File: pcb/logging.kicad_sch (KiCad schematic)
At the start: 14 parts, among them J6 MSD-4-A, U12 W25Q128JVS

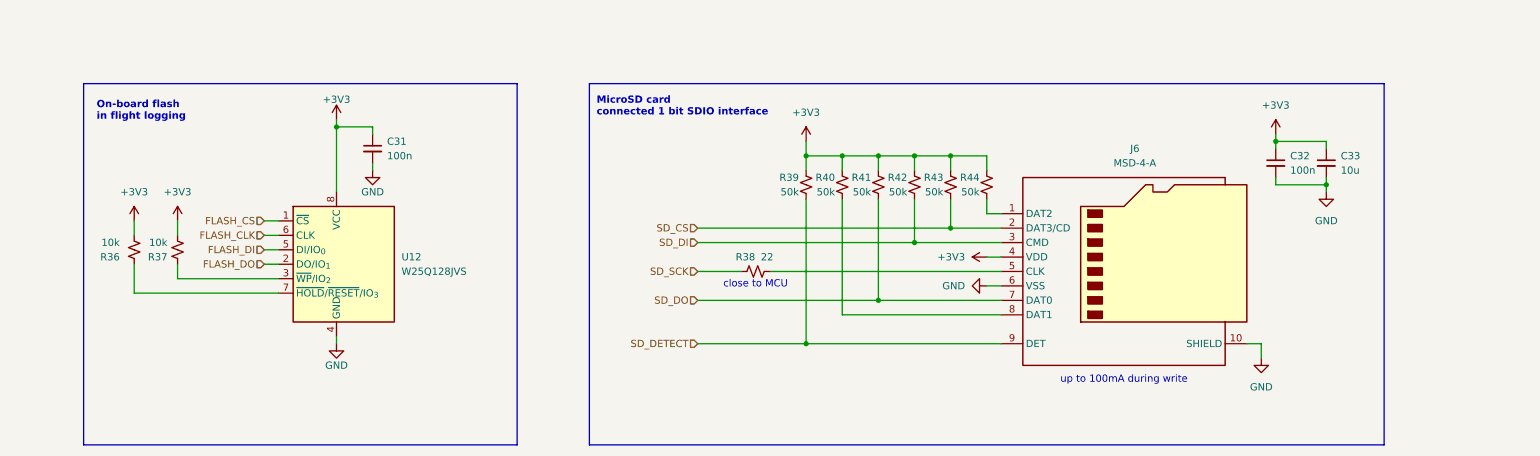
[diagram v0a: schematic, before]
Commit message: Improve inter sheet connections
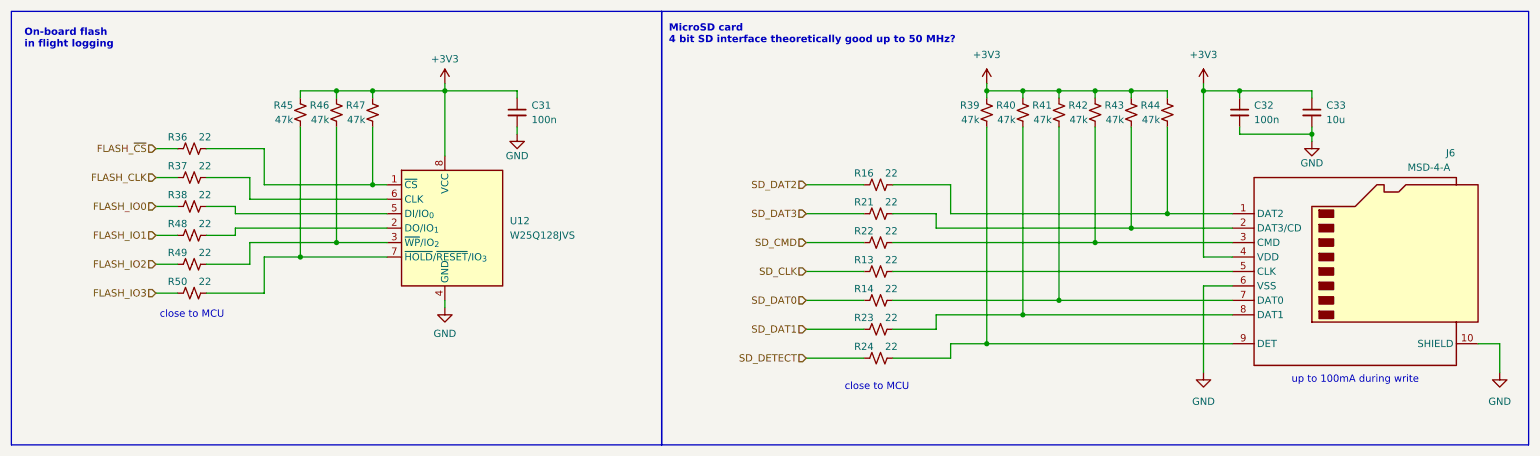
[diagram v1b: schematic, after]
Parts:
- added R13, R14, R16, R21, R22, R23, R24, R48, R49, R50: 22, symbol Device:R_Small_US
- added R45, R46, R47: 47k, symbol Device:R_Small_US
- R36, R37: value 10k -> 22
- R39, R40, R41, R42, R43, R44: value 50k -> 47k
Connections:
- net FLASH_DI is gone; now on an unnamed net: U12.5 (DI/IO_{0})
- net +3V3: now also R45.1, R46.1, R47.1; no longer R36.1, R37.1
- net FLASH_CLK: now also R37.1; no longer U12.6 (CLK)
- net SD_DETECT: now also R24.1; no longer J6.9 (DET), R39.2
- net at J6.1 (DAT2), R44.2: now also R16.2
- net at R38.2: no longer J6.5 (CLK)
- net at J6.8 (DAT1), R40.2: now also R23.2
- net at R37.2: now also U12.6 (CLK); no longer U12.3 (~{WP}/IO_{2})
- net at U12.7 (~{HOLD}/~{RESET}/IO_{3}): now also R45.2, R50.2; no longer R36.2
- net FLASH_CS: no longer names the net of U12.1 (~{CS})
- net FLASH_CS: now also R36.2, R47.2
- net FLASH_DO: no longer names the net of U12.2 (DO/IO_{1})
- net FLASH_DO: now also R48.2
- net SD_CS: no longer names the net of J6.2 (DAT3/CD), R43.2
- net SD_CS: now also R21.2
- net SD_DI: no longer names the net of J6.3 (CMD), R42.2
- net SD_DI: now also R22.2
- net SD_DO: no longer names the net of J6.7 (DAT0), R41.2
- net SD_DO: now also R14.2
- net SD_SCK renamed FLASH_IO0
- new net: R46.2, R49.2, U12.3 (~{WP}/IO_{2})
- new net: J6.9 (DET), R24.2, R39.2
- new net: J6.5 (CLK), R13.2
- new net FLASH_IO1: R48.1
- new net FLASH_IO2: R49.1
- new net FLASH_IO3: R50.1
- new net FLASH_~{CS}: R36.1
- new net SD_CLK: R13.1
- new net SD_CMD: R22.1
- new net SD_DAT0: R14.1
- new net SD_DAT1: R23.1
- new net SD_DAT2: R16.1
- new net SD_DAT3: R21.1
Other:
- note added: "MicroSD card 4 bit SD interface theoretically good up to 50 MHz?"
- note removed: "MicroSD card connected 1 bit SDIO interface"
- title: (none) -> Flight Computer
- moved on the sheet: C31, C32, C33, J6, R39, R40, R41, R42, R43, R44, U12

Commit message: Fix pin directionality
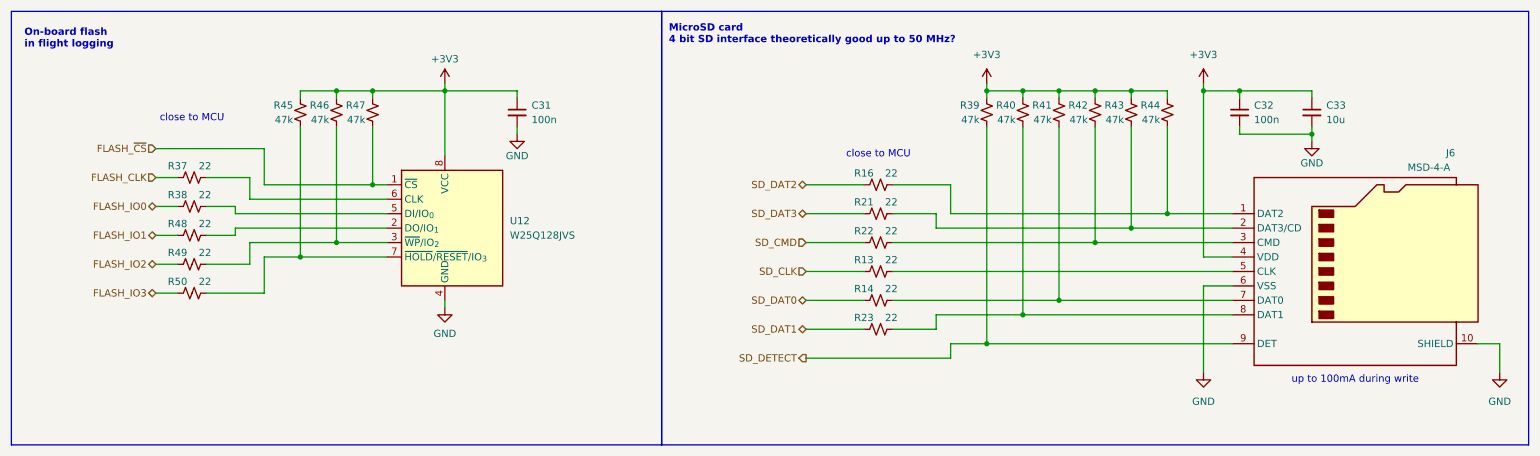
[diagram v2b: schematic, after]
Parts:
- removed R24, R36: 22, symbol Device:R_Small_US
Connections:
- net FLASH_~{CS}: now also R47.2, U12.1 (~{CS})
- net SD_DETECT: now also J6.9 (DET), R39.2
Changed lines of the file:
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@@
 	(text "close to MCU"
 		(exclude_from_sim no)
-		(at 44.45 66.04 0)
+		(at 44.45 31.496 0)
 		(effects
 			(font
@@
 	(text "close to MCU"
 		(exclude_from_sim no)
-		(at 164.846 78.74 0)
+		(at 165.1 37.846 0)
 		(effects
 			(font
@@
 	(wire
 		(pts
-			(xy 46.99 36.83) (xy 57.15 36.83)
-		)
-		(stroke
-			(width 0)
-			(type default)
-		)
-	)
-	(wire
-		(pts
 			(xy 167.64 63.5) (xy 196.85 63.5)
 		)
@@
 	(wire
 		(pts
-			(xy 38.1 36.83) (xy 41.91 36.83)
+			(xy 38.1 36.83) (xy 57.15 36.83)
 		)
 		(stroke
@@
 	(wire
 		(pts
-			(xy 152.4 73.66) (xy 162.56 73.66)
+			(xy 152.4 73.66) (xy 177.8 73.66)
 		)
 		(stroke
@@
 	(wire
 		(pts
-			(xy 167.64 73.66) (xy 177.8 73.66)
-		)
-		(stroke
-			(width 0)
-			(type default)
-		)
-	)
-	(wire
-		(pts
 			(xy 227.33 48.26) (xy 215.9 48.26)
 		)
@@
 	)
 	(hierarchical_label "SD_DETECT"
-		(shape input)
+		(shape output)
 		(at 152.4 73.66 180)
 		(effects
@@
 	)
 	(hierarchical_label "SD_DAT1"
-		(shape input)
+		(shape bidirectional)
 		(at 152.4 68.58 180)
 		(effects
@@
 	)
 	(hierarchical_label "FLASH_IO0"
-		(shape input)
+		(shape bidirectional)
 		(at 38.1 46.99 180)
 		(effects
@@
 	)
 	(hierarchical_label "FLASH_IO3"
-		(shape input)
+		(shape bidirectional)
 		(at 38.1 62.23 180)
 		(effects
@@
 	)
 	(hierarchical_label "FLASH_IO1"
-		(shape input)
+		(shape bidirectional)
 		(at 38.1 52.07 180)
 		(effects
@@
 	)
 	(hierarchical_label "SD_DAT3"
-		(shape input)
+		(shape bidirectional)
 		(at 152.4 48.26 180)
 		(effects
@@
 	)
 	(hierarchical_label "SD_DAT0"
-		(shape input)
+		(shape bidirectional)
 		(at 152.4 63.5 180)
 		(effects
@@
 	)
 	(hierarchical_label "FLASH_IO2"
-		(shape input)
+		(shape bidirectional)
 		(at 38.1 57.15 180)
 		(effects
@@
 	)
 	(hierarchical_label "SD_DAT2"
-		(shape input)
+		(shape bidirectional)
 		(at 152.4 43.18 180)
 		(effects
@@
 	)
 	(symbol
-		(lib_id "Device:R_Small_US")
-		(at 165.1 73.66 90)
-		(unit 1)
-		(exclude_from_sim no)
-		(in_bom yes)
-		(on_board yes)
-		(dnp no)
-		(property "Reference" "R24"
-			(at 162.56 71.628 90)
-			(effects
-				(font
-					(size 1.27 1.27)
-				)
-			)
-		)
-		(property "Value" "22"
-			(at 167.386 71.628 90)
-			(effects
-				(font
-					(size 1.27 1.27)
-				)
-			)
-		)
-		(property "Footprint" ""
-			(at 165.1 73.66 0)
-			(effects
-				(font
-					(size 1.27 1.27)
-				)
-				(hide yes)
-			)
-		)
-		(property "Datasheet" "~"
-			(at 165.1 73.66 0)
-			(effects
-				(font
-					(size 1.27 1.27)
-				)
-				(hide yes)
-			)
-		)
-		(property "Description" "Resistor, small US symbol"
-			(at 165.1 73.66 0)
-			(effects
-				(font
-					(size 1.27 1.27)
-				)
-				(hide yes)
-			)
-		)
-		(pin "2"
-		)
-		(pin "1"
-		)
-		(instances
-			(project "flight-computer"
-				(path "/84bf90ca-3018-4167-b21c-becfa336d24d/aa369500-0174-4f7d-8ef6-77a35d9b812a"
-					(reference "R24")
-					(unit 1)
-				)
-			)
-		)
-	)
-	(symbol
 		(lib_id "power:GND")
 		(at 274.32 76.2 0)
@@
 					(unit 1)
 				)
-			)
-		)
-	)
-	(symbol
-		(lib_id "Device:R_Small_US")
-		(at 44.45 36.83 90)
-		(unit 1)
-		(exclude_from_sim no)
-		(in_bom yes)
-		(on_board yes)
-		(dnp no)
-		(property "Reference" "R36"
-			(at 41.91 34.798 90)
-			(effects
-				(font
-					(size 1.27 1.27)
-				)
-			)
-		)
-		(property "Value" "22"
-			(at 46.736 34.798 90)
-			(effects
-				(font
-					(size 1.27 1.27)
-				)
-			)
-		)
-		(property "Footprint" ""
-			(at 44.45 36.83 0)
-			(effects
-				(font
-					(size 1.27 1.27)
-				)
-				(hide yes)
-			)
-		)
-		(property "Datasheet" "~"
-			(at 44.45 36.83 0)
-			(effects
-				(font
-					(size 1.27 1.27)
-				)
-				(hide yes)
-			)
-		)
-		(property "Description" "Resistor, small US symbol"
-			(at 44.45 36.83 0)
-			(effects
-				(font
-					(size 1.27 1.27)
-				)
-				(hide yes)
-			)
-		)
-		(pin "2"
-		)
-		(pin "1"
-		)
-		(instances
-			(project "flight-computer"
-				(path "/84bf90ca-3018-4167-b21c-becfa336d24d/aa369500-0174-4f7d-8ef6-77a35d9b812a"
-					(reference "R36")
-					(unit 1)
-				)

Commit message: Assign most footprints
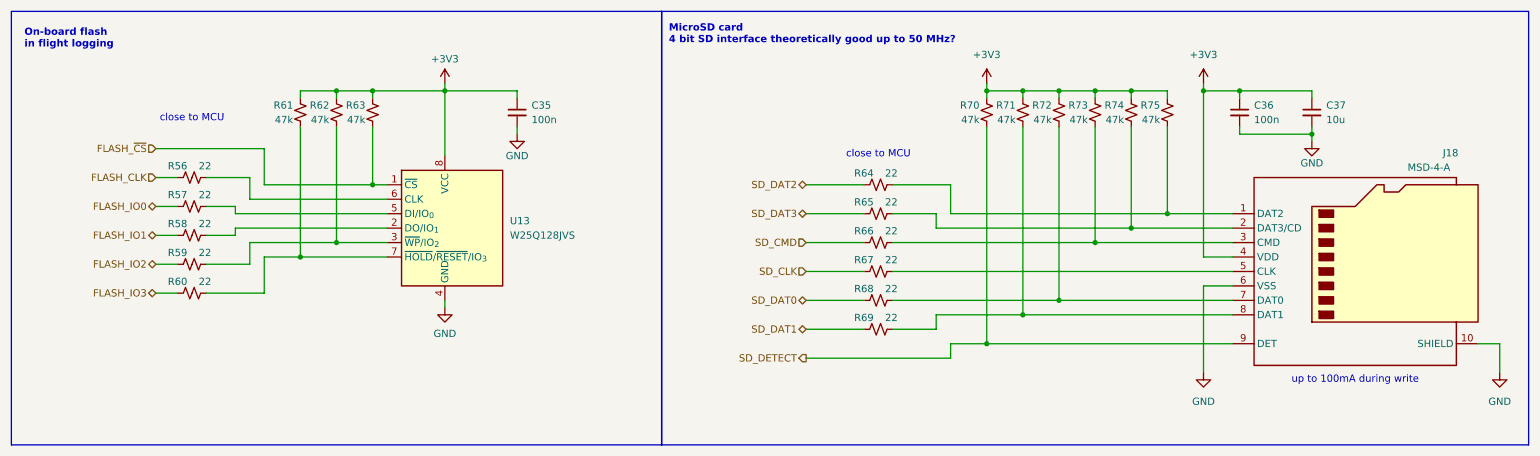
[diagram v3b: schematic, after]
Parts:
- C35: renamed from C31; footprint (none) -> Capacitor_SMD:C_0603_1608Metric
- C36: renamed from C32; footprint (none) -> Capacitor_SMD:C_0603_1608Metric
- C37: renamed from C33; footprint (none) -> Capacitor_SMD:C_0603_1608Metric
- R56: renamed from R37; footprint (none) -> Resistor_SMD:R_0603_1608Metric
- R57: renamed from R38; footprint (none) -> Resistor_SMD:R_0603_1608Metric
- R58: renamed from R48; footprint (none) -> Resistor_SMD:R_0603_1608Metric
- R59: renamed from R49; footprint (none) -> Resistor_SMD:R_0603_1608Metric
- R60: renamed from R50; footprint (none) -> Resistor_SMD:R_0603_1608Metric
- R61: renamed from R45; footprint (none) -> Resistor_SMD:R_0603_1608Metric
- R62: renamed from R46; footprint (none) -> Resistor_SMD:R_0603_1608Metric
- R63: renamed from R47; footprint (none) -> Resistor_SMD:R_0603_1608Metric
- R64: renamed from R16; footprint (none) -> Resistor_SMD:R_0603_1608Metric
- R65: renamed from R21; footprint (none) -> Resistor_SMD:R_0603_1608Metric
- R66: renamed from R22; footprint (none) -> Resistor_SMD:R_0603_1608Metric
- R67: renamed from R13; footprint (none) -> Resistor_SMD:R_0603_1608Metric
- R68: renamed from R14; footprint (none) -> Resistor_SMD:R_0603_1608Metric
- R69: renamed from R23; footprint (none) -> Resistor_SMD:R_0603_1608Metric
- R70: renamed from R39; footprint (none) -> Resistor_SMD:R_0603_1608Metric
- R71: renamed from R40; footprint (none) -> Resistor_SMD:R_0603_1608Metric
- R72: renamed from R41; footprint (none) -> Resistor_SMD:R_0603_1608Metric
- R73: renamed from R42; footprint (none) -> Resistor_SMD:R_0603_1608Metric
- R74: renamed from R43; footprint (none) -> Resistor_SMD:R_0603_1608Metric
- R75: renamed from R44; footprint (none) -> Resistor_SMD:R_0603_1608Metric
- renumbered J6 to J18, U12 to U13
